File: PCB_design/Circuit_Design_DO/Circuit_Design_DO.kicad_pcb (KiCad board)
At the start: 4 copper layers, 113 parts, among them J1 Conn_Coaxial, J2 USB_C_Receptacle_USB2.0_16P, J3 ICSP, K1 SANYOU_SRD_Form_A, Q2 SS8050, SW1 SW_Push, SW2 RotaryEncoder, SW3 RotaryEncoder, SW4 SW_Push, U1 AMC3330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

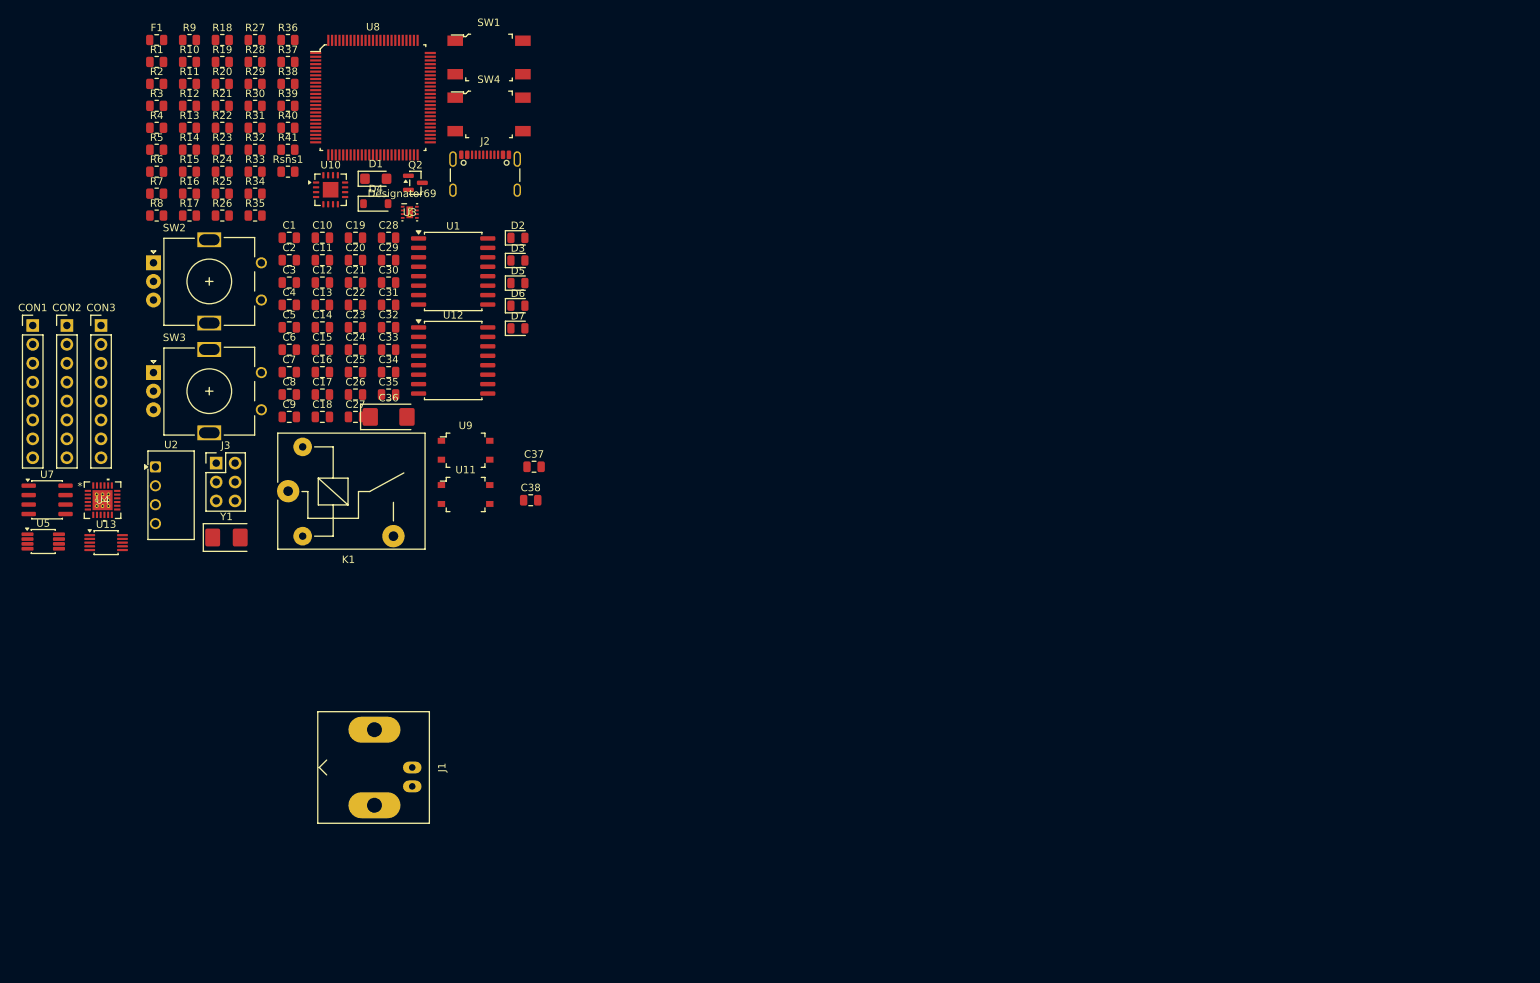
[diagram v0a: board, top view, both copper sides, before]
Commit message: Added a folder for a normal pcb design, the other one is Arduino style, started an Arduino PCB layout with headers, repaired schematic mistakes
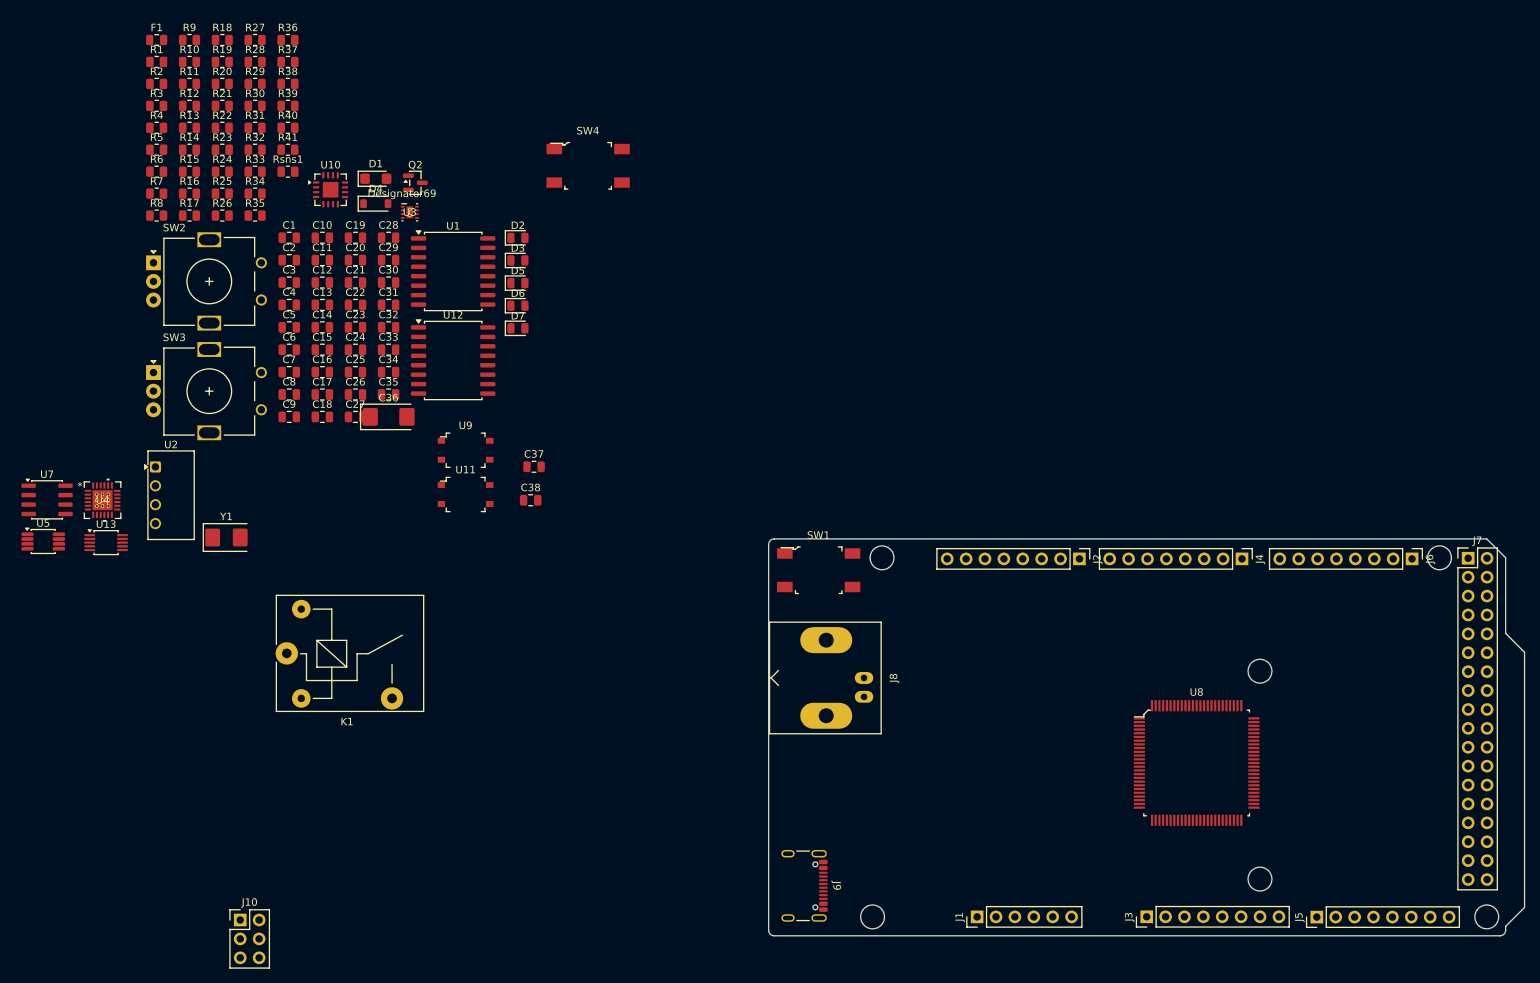
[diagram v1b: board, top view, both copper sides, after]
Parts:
- removed CON1, CON2, CON3: ~, Connector_PinHeader_2.54mm:PinHeader_1x08_P2.54mm_Vertical
- added ?: , , F.Cu at (214.0, 136.0)
- added ?: , , F.Cu at (132.7, 87.7)
- added ?: , , F.Cu at (207.7, 87.7)
- added ?: , , F.Cu at (131.4, 136.0)
- added ?: , , F.Cu at (183.5, 130.9)
- added ?: , , F.Cu at (183.5, 103.0)
- added J10: ICSP, Connector_PinHeader_2.54mm:PinHeader_2x03_P2.54mm_Vertical, F.Cu at (46.5, 136.4)
- added J4: PWM, Connector_PinHeader_2.54mm:PinHeader_1x08_P2.54mm_Vertical, F.Cu at (181.1, 87.9)
- added J5: Analog, Connector_PinHeader_2.54mm:PinHeader_1x08_P2.54mm_Vertical, F.Cu at (191.2, 136.0)
- added J6: COMUNICATION, Connector_PinHeader_2.54mm:PinHeader_1x08_P2.54mm_Vertical, F.Cu at (204.0, 87.9)
- added J7: Digital, Connector_PinHeader_2.54mm:PinHeader_2x18_P2.54mm_Vertical, F.Cu at (211.5, 87.8)
- added J8: Conn_Coaxial, Connector_Coaxial:BNC_Amphenol_B6252HB-NPP3G-50_Horizontal, F.Cu at (130.3, 103.9)
- added J9: USB_C_Receptacle_USB2.0_16P, Connector_USB:USB_C_Receptacle_GCT_USB4105-xx-A_16P_TopMnt_Horizontal, F.Cu at (121.2, 131.8)
- J1: value Conn_Coaxial -> Power; footprint Connector_Coaxial:BNC_Amphenol_B6252HB-NPP3G-50_Horizontal -> Connector_PinHeader_2.54mm:PinHeader_1x06_P2.54mm_Vertical
- J2: value USB_C_Receptacle_USB2.0_16P -> ~; footprint Connector_USB:USB_C_Receptacle_GCT_USB4105-xx-A_16P_TopMnt_Horizontal -> Connector_PinHeader_2.54mm:PinHeader_1x08_P2.54mm_Vertical
- J3: value ICSP -> Analog; footprint Connector_PinHeader_2.54mm:PinHeader_2x03_P2.54mm_Vertical -> Connector_PinHeader_2.54mm:PinHeader_1x08_P2.54mm_Vertical
- SW1: value SW_Push -> SW_Reset
- moved U8 142.3 mm to (175.0, 115.3)
- moved J3 139.1 mm to (168.3, 136.0), turned to 90 degrees
- moved J2 94.6 mm to (159.3, 87.9), turned to -90 degrees
- moved SW1 81.9 mm to (124.2, 89.4)
- moved J1 78.5 mm to (145.5, 136.0)
- moved K1 21.8 mm to (52.7, 100.6)
- moved SW4 15.0 mm to (93.2, 35.1)
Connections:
- net Net-(U8A-PD0(SCL/INT0)) renamed /PD0
- net Net-(U8A-PD1(SDA/INT1)) renamed /PD1
- net Net-(U8A-PD2(RXD1/INT2)) renamed /PD2
- net Net-(U8A-PD3(TXD1/INT3)) renamed /PD3
- D3 pad 2: Net-(D3-A) -> /PB7
- J1 pad 1: Net-(J1-In) -> rst_dn
- J1 pad 2: Net-(J1-Ext) -> +5VD
- J3 pad 1: /MISO_D -> Net-(U8A-PF0(ADC0))
- J3 pad 2: +5VD -> Net-(U8A-PF1(ADC1))
- J3 pad 3: /SCK_D -> Net-(U8A-PF2(ADC2))
- J3 pad 4: /MOSI_D -> Net-(U8A-PF3(ADC3))
- J3 pad 5: rst_dn -> Net-(U8A-PF4(ADC4/TCK))
- J3 pad 6: DGND -> Net-(U8A-PF5(ADC5/TMS))
- R1 pad 1: Net-(J1-In) -> Net-(J8-In)
- R10 pad 1: Net-(J2-CC1) -> Net-(J9-CC1)
- R10 pad 2: Net-(J2-SHIELD) -> DGND
- R11 pad 1: Net-(J2-CC2) -> Net-(J9-CC2)
- R11 pad 2: Net-(J2-SHIELD) -> DGND
- R3 pad 2: Net-(J1-Ext) -> Net-(J8-Ext)
- U12 pad 4: /SCK_D -> /PB1
- U4 pad 1: StartConversion -> /CS_D
- U8 pad 1: unconnected-(U8A-PG5(OC08)-Pad1) -> /PG5
- U8 pad 12: unconnected-(U8A-PH0(RXD2)-Pad12) -> /PH0
- U8 pad 13: unconnected-(U8A-PH1(TXD2)-Pad13) -> /PH1
- U8 pad 14: unconnected-(U8A-PH2(XCK2)-Pad14) -> /PH2
- U8 pad 15: unconnected-(U8A-PH3(OC4A)-Pad15) -> /PH3
- U8 pad 16: unconnected-(U8A-PH4(OC4B)-Pad16) -> /PH4
- U8 pad 17: unconnected-(U8A-PH5(OC4C)-Pad17) -> /PH5
- U8 pad 18: unconnected-(U8A-PH6(OC2B)-Pad18) -> /PH6
- U8 pad 19: /CS_D -> /PB0
- U8 pad 20: /SCK_D -> /PB1
- U8 pad 23: unconnected-(U8A-PB4(OC2A/PCINT4)-Pad23) -> /CS_D
- U8 pad 24: unconnected-(U8A-PB5(OC1A/PCINT5)-Pad24) -> /PB5
- U8 pad 25: unconnected-(U8A-PB6(OC1B/PCINT6)-Pad25) -> /PB6
- U8 pad 26: Net-(D3-A) -> /PB7
- U8 pad 27: unconnected-(U8A-PH7(T4)-Pad27) -> /PH7
- U8 pad 28: unconnected-(U8A-PG3(TOSC2)-Pad28) -> /PG3
- U8 pad 29: unconnected-(U8A-PG4(TOSC1)-Pad29) -> /PG4
- U8 pad 35: unconnected-(U8A-PL0(ICP4)-Pad35) -> /PL0
- U8 pad 36: unconnected-(U8A-PL1(ICP5)-Pad36) -> /PL1
- U8 pad 37: unconnected-(U8A-PL2(T5)-Pad37) -> /PL2
- U8 pad 38: unconnected-(U8A-PL3(OC5A)-Pad38) -> /PL3
- U8 pad 39: unconnected-(U8A-PL4(OC5B)-Pad39) -> /PL4
- U8 pad 40: unconnected-(U8A-PL5(OC5C)-Pad40) -> /PL5
- U8 pad 41: unconnected-(U8A-PL6-Pad41) -> /PL6
- U8 pad 42: unconnected-(U8A-PL7-Pad42) -> /PL7
- U8 pad 47: unconnected-(U8A-PD4(ICP1)-Pad47) -> /PD4
- U8 pad 48: unconnected-(U8A-PD5(XCK1)-Pad48) -> /PD5
- U8 pad 49: unconnected-(U8A-PD6(T1)-Pad49) -> /PD6
- U8 pad 5: unconnected-(U8A-PE3(OC3A/AIN1)-Pad5) -> /PE3
- U8 pad 50: unconnected-(U8A-PD7(T0)-Pad50) -> /PD7
- U8 pad 51: unconnected-(U8A-PG0(~{WR})-Pad51) -> /PG0
- U8 pad 52: unconnected-(U8A-PG1(~{RD})-Pad52) -> /PG1
- U8 pad 53: Net-(U8A-PC0(A8)) -> /PC0
- U8 pad 54: Net-(U8A-PC1(A9)) -> /PC1
- U8 pad 55: Net-(U8A-PC2(A10)) -> /PC2
- U8 pad 56: Net-(U8A-PC3(A11)) -> /PC3
- U8 pad 57: Net-(U8A-PC4(A12)) -> /PC4
- U8 pad 58: Net-(U8A-PC5(A13)) -> /PC5
- U8 pad 59: Net-(U8A-PC6(A14)) -> /PC6
- U8 pad 60: Net-(U8A-PC7(A15)) -> /PC7
- U8 pad 63: unconnected-(U8A-PJ0(RXD3/PCINT9)-Pad63) -> /PJ0
- U8 pad 64: unconnected-(U8A-PJ1(TXD3/PCINT10)-Pad64) -> /PJ1
- U8 pad 65: unconnected-(U8A-PJ2(XCK3/PCINT11)-Pad65) -> /PJ2
- U8 pad 66: unconnected-(U8A-PJ3(PCINT12)-Pad66) -> /PJ3
- U8 pad 67: unconnected-(U8A-PJ4(PCINT13)-Pad67) -> /PJ4
- U8 pad 68: unconnected-(U8A-PJ5(PCINT14)-Pad68) -> /PJ5
- U8 pad 69: unconnected-(U8A-PJ6(PCINT15)-Pad69) -> /PJ6
- U8 pad 7: unconnected-(U8A-PE5(OC3C/INT5)-Pad7) -> /PE5
- U8 pad 70: unconnected-(U8A-PG2(ALE)-Pad70) -> /PG2
- U8 pad 71: unconnected-(U8A-PA7(AD7)-Pad71) -> /PA7
- U8 pad 72: unconnected-(U8A-PA6(AD6)-Pad72) -> /PA6
- U8 pad 73: unconnected-(U8A-PA5(AD5)-Pad73) -> /PA5
- U8 pad 74: unconnected-(U8A-PA4(AD4)-Pad74) -> /PA4
- U8 pad 75: unconnected-(U8A-PA3(AD3)-Pad75) -> /PA3
- U8 pad 76: unconnected-(U8A-PA2(AD2)-Pad76) -> /PA2
- U8 pad 79: unconnected-(U8A-PJ7-Pad79) -> /PJ7
- U8 pad 8: unconnected-(U8A-PE6(T3/INT6)-Pad8) -> /PE6
- U8 pad 9: unconnected-(U8A-PE7(CLKO/ICP3/INT7)-Pad9) -> /PE7
- U8 pad 98: unconnected-(U8A-AREF-Pad98) -> /AREF
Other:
- board outline added: 101.6 x 53.3 mm
